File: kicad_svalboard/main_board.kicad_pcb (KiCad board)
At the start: 2 copper layers, 42 x 67 mm, 35 parts, among them J1 Conn_01x07, J2 Conn_01x07, J3 Conn_01x07, J4 Conn_01x07, J5 Conn_01x07, J6 PJ-320D, J8 Conn_01x07, Q1 Q_NPN_BEC, Q2 Q_NPN_BEC, Q3 Q_NPN_BEC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

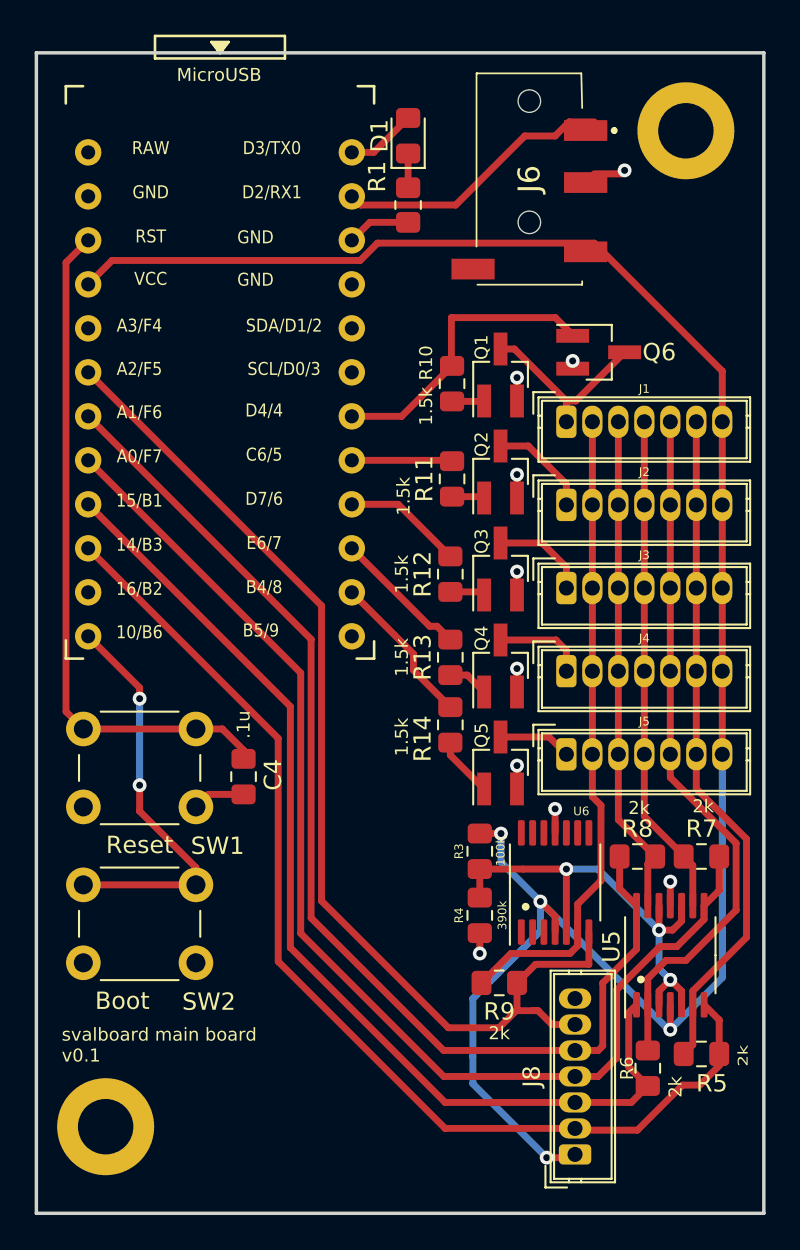
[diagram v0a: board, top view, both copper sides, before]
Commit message: Removed datasheets folder, updated design with layouts for cluster and main PCB.  still need FFC connectors on main PCB
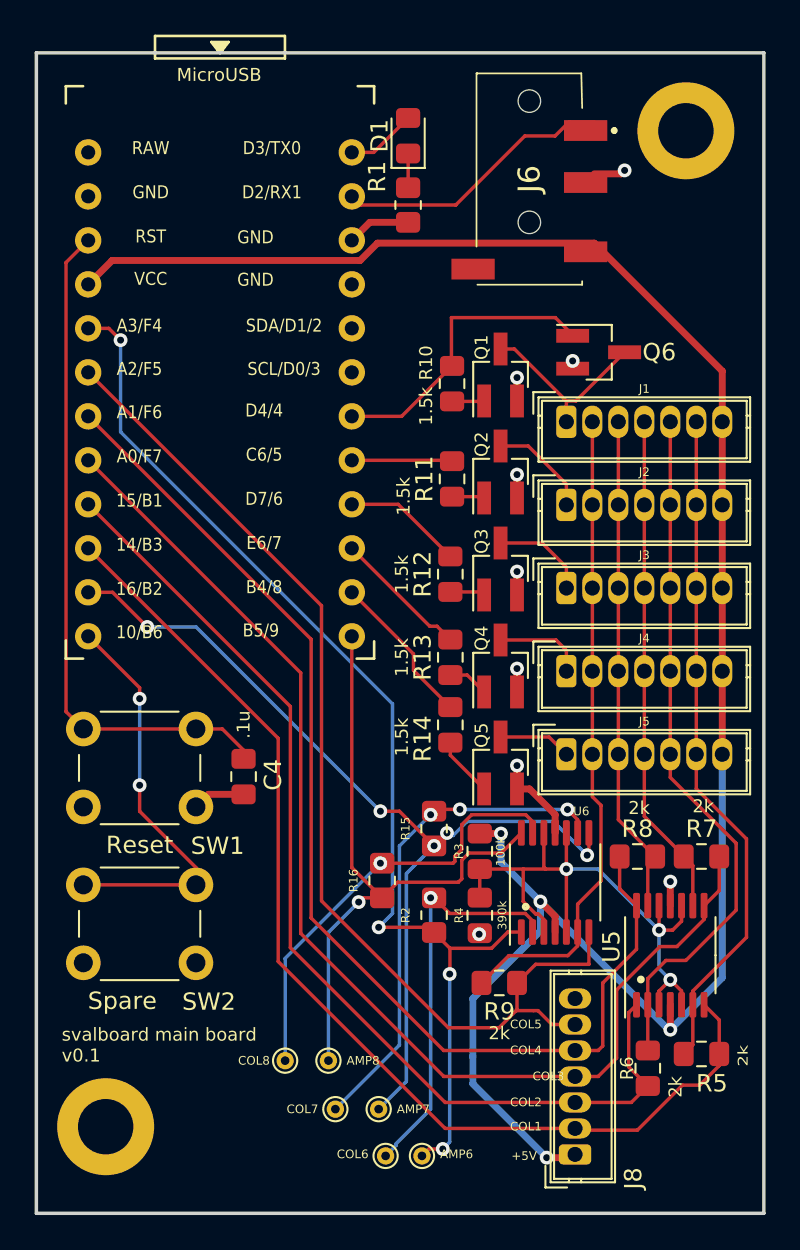
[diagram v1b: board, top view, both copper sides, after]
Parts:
- added AMP6: TestPoint, TestPoint:TestPoint_THTPad_D1.0mm_Drill0.5mm, F.Cu at (149.3, 124.4)
- added AMP7: TestPoint, TestPoint:TestPoint_THTPad_D1.0mm_Drill0.5mm, F.Cu at (146.8, 121.7)
- added AMP8: TestPoint, TestPoint:TestPoint_THTPad_D1.0mm_Drill0.5mm, F.Cu at (143.9, 118.9)
- added COL6: TestPoint, TestPoint:TestPoint_THTPad_D1.0mm_Drill0.5mm, F.Cu at (147.2, 124.4)
- added COL7: TestPoint, TestPoint:TestPoint_THTPad_D1.0mm_Drill0.5mm, F.Cu at (144.3, 121.7)
- added COL8: TestPoint, TestPoint:TestPoint_THTPad_D1.0mm_Drill0.5mm, F.Cu at (141.4, 118.9)
- added R15: 2k, Resistor_SMD:R_0805_2012Metric_Pad1.20x1.40mm_HandSolder, F.Cu at (150.0, 105.5)
- added R16: 2k, Resistor_SMD:R_0805_2012Metric_Pad1.20x1.40mm_HandSolder, F.Cu at (147.0, 108.5)
- added R2: 2k, Resistor_SMD:R_0805_2012Metric_Pad1.20x1.40mm_HandSolder, F.Cu at (150.0, 110.5)
- SW2: value Boot -> Spare
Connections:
- U1 pad 12: unconnected-(U1-Pad12) -> /COL8_AMP
- U1 pad 14: unconnected-(U1-Pad14) -> /COL7_AMP
- U1 pad 20: unconnected-(U1-Pad20) -> /COL6_AMP
- U6 pad 1: (no net) -> /COL6_AMP
- U6 pad 10: (no net) -> /AMP_REF
- U6 pad 12: (no net) -> /AMP_REF
- U6 pad 13: (no net) -> /COL8
- U6 pad 14: (no net) -> /COL8_AMP
- U6 pad 2: (no net) -> /COL6
- U6 pad 3: (no net) -> /AMP_REF
- U6 pad 8: (no net) -> /COL7_AMP
- U6 pad 9: (no net) -> /COL7
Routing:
- net /COL6_AMP: track 0.00 -> 65.1 mm, vias 0 -> 4
- net /COL7_AMP: track 0.00 -> 54.2 mm, vias 0 -> 5
- net /COL8_AMP: track 0.00 -> 37.4 mm, vias 0 -> 1
- net /COL7: track 0.00 -> 28.9 mm, vias 0 -> 3
- net /COL8: track 0.00 -> 25.5 mm, vias 0 -> 1
- net /COL6: track 0.00 -> 23.1 mm, vias 0 -> 1
- net /AMP_REF: track 27.5 -> 35.9 mm
- net GND: track 19.7 -> 22.1 mm, vias 10 -> 9
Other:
- board text added: "+5V"
- board text added: "COL1"
- board text added: "COL2"
- board text added: "COL3"
- board text added: "COL4"
- board text added: "COL5"
